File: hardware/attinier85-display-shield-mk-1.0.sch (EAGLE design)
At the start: 5 parts, among them U1 ATTINIEST85_SHIELDV2

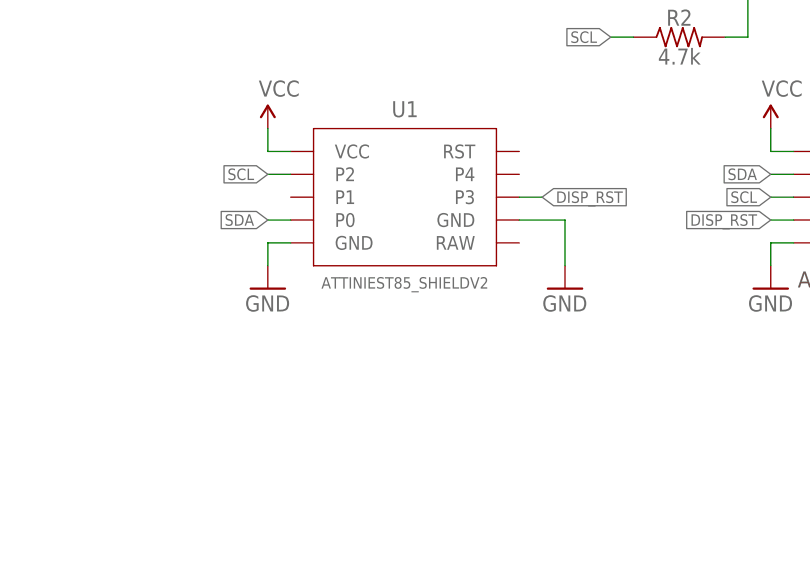
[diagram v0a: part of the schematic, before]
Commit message: renaming parts
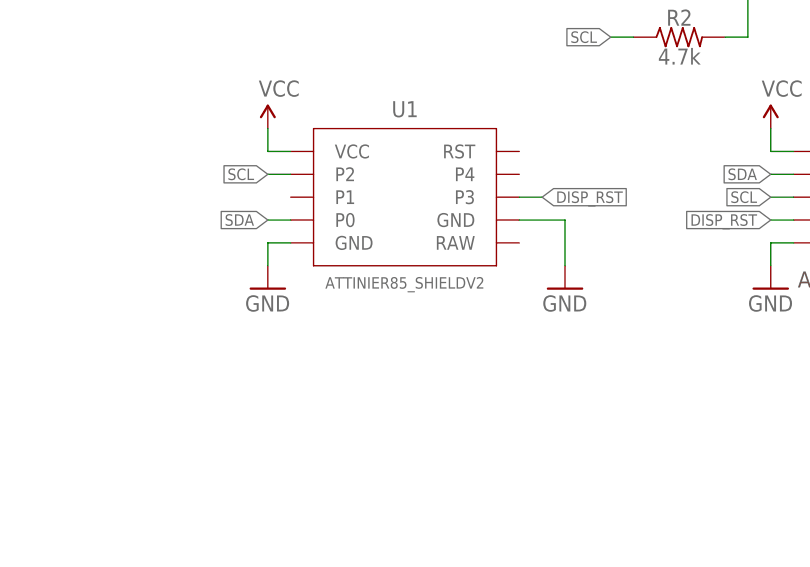
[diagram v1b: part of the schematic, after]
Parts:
- U1: value ATTINIEST85_SHIELDV2 -> ATTINIER85_SHIELDV2; device A_butts:ATTINIEST85_SHIELDV2 -> A_butts:ATTINIER85_SHIELDV2
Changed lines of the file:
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@@
 <grid distance="100" unitdist="mil" unit="mil" style="lines" multiple="1" display="yes" altdistance="2" altunitdist="mil" altunit="mil"/>
 <layers>
-<layer number="1" name="Top" color="4" fill="1" visible="yes" active="no"/>
-<layer number="16" name="Bottom" color="1" fill="1" visible="yes" active="no"/>
-<layer number="17" name="Pads" color="2" fill="1" visible="yes" active="no"/>
-<layer number="18" name="Vias" color="2" fill="1" visible="yes" active="no"/>
-<layer number="19" name="Unrouted" color="6" fill="1" visible="yes" active="no"/>
-<layer number="20" name="Dimension" color="15" fill="1" visible="yes" active="no"/>
-<layer number="21" name="tPlace" color="7" fill="1" visible="yes" active="no"/>
-<layer number="22" name="bPlace" color="7" fill="1" visible="yes" active="no"/>
-<layer number="23" name="tOrigins" color="15" fill="1" visible="yes" active="no"/>
-<layer number="24" name="bOrigins" color="15" fill="1" visible="yes" active="no"/>
-<layer number="25" name="tNames" color="7" fill="1" visible="yes" active="no"/>
-<layer number="26" name="bNames" color="7" fill="1" visible="yes" active="no"/>
-<layer number="27" name="tValues" color="7" fill="1" visible="yes" active="no"/>
-<layer number="28" name="bValues" color="7" fill="1" visible="yes" active="no"/>
+<layer number="1" name="Top" color="4" fill="1" visible="no" active="no"/>
+<layer number="16" name="Bottom" color="1" fill="1" visible="no" active="no"/>
+<layer number="17" name="Pads" color="2" fill="1" visible="no" active="no"/>
+<layer number="18" name="Vias" color="2" fill="1" visible="no" active="no"/>
+<layer number="19" name="Unrouted" color="6" fill="1" visible="no" active="no"/>
+<layer number="20" name="Dimension" color="15" fill="1" visible="no" active="no"/>
+<layer number="21" name="tPlace" color="7" fill="1" visible="no" active="no"/>
+<layer number="22" name="bPlace" color="7" fill="1" visible="no" active="no"/>
+<layer number="23" name="tOrigins" color="15" fill="1" visible="no" active="no"/>
+<layer number="24" name="bOrigins" color="15" fill="1" visible="no" active="no"/>
+<layer number="25" name="tNames" color="7" fill="1" visible="no" active="no"/>
+<layer number="26" name="bNames" color="7" fill="1" visible="no" active="no"/>
+<layer number="27" name="tValues" color="7" fill="1" visible="no" active="no"/>
+<layer number="28" name="bValues" color="7" fill="1" visible="no" active="no"/>
 <layer number="29" name="tStop" color="7" fill="3" visible="no" active="no"/>
 <layer number="30" name="bStop" color="7" fill="6" visible="no" active="no"/>
@@
 <layer number="35" name="tGlue" color="7" fill="4" visible="no" active="no"/>
 <layer number="36" name="bGlue" color="7" fill="5" visible="no" active="no"/>
-<layer number="37" name="tTest" color="7" fill="1" visible="yes" active="no"/>
-<layer number="38" name="bTest" color="7" fill="1" visible="yes" active="no"/>
+<layer number="37" name="tTest" color="7" fill="1" visible="no" active="no"/>
+<layer number="38" name="bTest" color="7" fill="1" visible="no" active="no"/>
 <layer number="39" name="tKeepout" color="4" fill="11" visible="no" active="no"/>
 <layer number="40" name="bKeepout" color="1" fill="11" visible="no" active="no"/>
@@
 <layer number="44" name="Drills" color="7" fill="1" visible="no" active="no"/>
 <layer number="45" name="Holes" color="7" fill="1" visible="no" active="no"/>
-<layer number="46" name="Milling" color="3" fill="1" visible="yes" active="no"/>
-<layer number="47" name="Measures" color="7" fill="1" visible="yes" active="no"/>
-<layer number="48" name="Document" color="7" fill="1" visible="yes" active="no"/>
-<layer number="49" name="Reference" color="7" fill="1" visible="yes" active="no"/>
-<layer number="50" name="dxf" color="7" fill="1" visible="yes" active="no"/>
-<layer number="51" name="tDocu" color="7" fill="1" visible="yes" active="no"/>
-<layer number="52" name="bDocu" color="7" fill="1" visible="yes" active="no"/>
-<layer number="53" name="tGND_GNDA" color="7" fill="9" visible="yes" active="no"/>
-<layer number="54" name="bGND_GNDA" color="1" fill="9" visible="yes" active="no"/>
-<layer number="56" name="wert" color="7" fill="1" visible="yes" active="no"/>
-<layer number="57" name="tCAD" color="7" fill="1" visible="yes" active="no"/>
+<layer number="46" name="Milling" color="3" fill="1" visible="no" active="no"/>
+<layer number="47" name="Measures" color="7" fill="1" visible="no" active="no"/>
+<layer number="48" name="Document" color="7" fill="1" visible="no" active="no"/>
+<layer number="49" name="Reference" color="7" fill="1" visible="no" active="no"/>
+<layer number="50" name="dxf" color="7" fill="1" visible="no" active="no"/>
+<layer number="51" name="tDocu" color="7" fill="1" visible="no" active="no"/>
+<layer number="52" name="bDocu" color="7" fill="1" visible="no" active="no"/>
+<layer number="53" name="tGND_GNDA" color="7" fill="9" visible="no" active="no"/>
+<layer number="54" name="bGND_GNDA" color="1" fill="9" visible="no" active="no"/>
+<layer number="56" name="wert" color="7" fill="1" visible="no" active="no"/>
+<layer number="57" name="tCAD" color="7" fill="1" visible="no" active="no"/>
 <layer number="90" name="Modules" color="5" fill="1" visible="yes" active="yes"/>
 <layer number="91" name="Nets" color="2" fill="1" visible="yes" active="yes"/>
@@
 <parts>
 <part name="FRAME1" library="A_butts" deviceset="FRAME-LETTER" device="NO_PACKAGE"/>
-<part name="U1" library="A_butts" deviceset="ATTINIEST85_SHIELD" device="V2"/>
+<part name="U1" library="A_butts" deviceset="ATTINIER85_SHIELD" device="V2"/>
 <part name="SUPPLY1" library="A_butts" deviceset="VCC" device=""/>
 <part name="GND1" library="A_butts" deviceset="GND" device=""/>

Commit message: cleaning up version spoo
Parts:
- added I2C: M04PTH, A_butts:M04PTH
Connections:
- net GND: now also I2C.1
- net SCL: now also I2C.4
- net SDA: now also I2C.3
- net VCC: now also I2C.2
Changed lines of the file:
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@@
 <part name="R2" library="A_butts" deviceset="RESISTOR" device="PTH-AXIAL-7.62MM" value="4.7k"/>
 <part name="SUPPLY3" library="A_butts" deviceset="VCC" device=""/>
+<part name="SUPPLY4" library="A_butts" deviceset="VCC" device=""/>
+<part name="GND4" library="A_butts" deviceset="GND" device=""/>
+<part name="I2C" library="A_butts" deviceset="M04" device="PTH" value="M04PTH"/>
 </parts>
 <sheets>
@@
 <instance part="R2" gate="G$1" x="93.98" y="91.44"/>
 <instance part="SUPPLY3" gate="G$1" x="101.6" y="101.6"/>
+<instance part="SUPPLY4" gate="G$1" x="116.84" y="121.92"/>
+<instance part="GND4" gate="1" x="116.84" y="99.06"/>
+<instance part="I2C" gate="G$1" x="132.08" y="111.76" rot="MR0"/>
 </instances>
 <busses>
@@
 <wire x1="104.14" y1="68.58" x2="106.68" y2="68.58" width="0.1524" layer="91"/>
 <pinref part="GND3" gate="1" pin="GND"/>
+</segment>
+<segment>
+<pinref part="GND4" gate="1" pin="GND"/>
+<wire x1="116.84" y1="101.6" x2="116.84" y2="109.22" width="0.1524" layer="91"/>
+<wire x1="116.84" y1="109.22" x2="127" y2="109.22" width="0.1524" layer="91"/>
+<pinref part="I2C" gate="G$1" pin="1"/>
 </segment>
 </net>
@@
 <junction x="101.6" y="99.06"/>
 </segment>
+<segment>
+<pinref part="SUPPLY4" gate="G$1" pin="VCC"/>
+<wire x1="116.84" y1="121.92" x2="116.84" y2="111.76" width="0.1524" layer="91"/>
+<wire x1="116.84" y1="111.76" x2="127" y2="111.76" width="0.1524" layer="91"/>
+<pinref part="I2C" gate="G$1" pin="2"/>
+</segment>
 </net>
 <net name="SDA" class="0">
@@
 <label x="86.36" y="99.06" size="1.27" layer="95" rot="R180" xref="yes"/>
 <pinref part="R1" gate="G$1" pin="1"/>
+</segment>
+<segment>
+<wire x1="124.46" y1="114.3" x2="127" y2="114.3" width="0.1524" layer="91"/>
+<label x="124.46" y="114.3" size="1.27" layer="95" rot="R180" xref="yes"/>
+<pinref part="I2C" gate="G$1" pin="3"/>
 </segment>
 </net>
@@
 <pinref part="R2" gate="G$1" pin="1"/>
 </segment>
+<segment>
+<wire x1="124.46" y1="116.84" x2="127" y2="116.84" width="0.1524" layer="91"/>
+<label x="124.46" y="116.84" size="1.27" layer="95" rot="R180" xref="yes"/>
+<pinref part="I2C" gate="G$1" pin="4"/>
+</segment>
 </net>
